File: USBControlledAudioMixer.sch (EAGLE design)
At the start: 36 parts, among them IC1 TDA7448, IC2 TS912, IC3 MEGA8-AI, J1 MOLEX 47346-0001, J2 AVR_SPI_PRG_6NS

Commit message: Minor update (sorry for nonsense commit message)
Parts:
- removed D2: BZX84CSMD, diode:BZX84CSMD
- removed LED6, LED7, LED8: (no value), led:LEDCHIPLED-0603-TTW
- added D3: (no value), diode:DIODE-2CA|ACSOT23
- added IC4: OPA344N-SOT23, linear:OPA344N-SOT23
- added JP1: (no value), pinhead:PINHD-1X4/90
- added L1: (no value), rcl:L-EUL3225M
- added R10, R11, R6, R7, R8, R9: (no value), rcl:R-EU_R0603
- added R12: 470, rcl:R-EU_R0603
- added R13, R14: 62, rcl:R-EU_R0603
- added R15: 1k5, rcl:R-EU_R0603
- added U$1: 470, Simplex-rlc:RES_ARR
- C1: value 22p -> 12p; device rcl:C-EUC0805K -> rcl:C-EUC0603; OC_DIGIKEY (none) -> 1276-1254-1-ND; OC_TME CL21C220JBANNNC -> (none); PRICE_100 (none) -> 0.013
- C10, C11, C6, C7, C8, C9: value 22p -> 470n; device rcl:C-EUC0805K -> rcl:C-EUC0603; OC_DIGIKEY (none) -> 1276-2377-1-ND; OC_TME CL21C220JBANNNC -> (none); PRICE_100 (none) -> 0.017
- C2: value 22p -> 12p; device rcl:C-EUC0805K -> rcl:C-EUC0603
- C3: device rcl:C-EUC0805K -> rcl:C-EUC0603; OC_DIGIKEY (none) -> 1276-1258-1-ND; OC_TME CC0805JRX7R9104 -> (none); PRICE_100 (none) -> 0.008
- C4: device rcl:CPOL-EUA/3216-18W -> rcl:CPOL-EUSMCA; OC_TME TAJA106M010R -> TAJA155K016R; PRICE_100 (none) -> 0.059
- D1: value BZX84CSMD -> (none); device diode:BZX84CSMD -> diode:DIODE-SOD123; OC_TME BZX84C3V6-DIO -> (none)
- IC3: OC_TME (none) -> ATMEGA8-16AU; PRICE_10 (none) -> 1.37
- LED1, LED2, LED3, LED4, LED5: OC_TME (none) -> KPA-1606QBC-F; PRICE_100 (none) -> 0.2511
- Q1: value (none) -> 16MHz; device crystal:CRYSTALHC49UP -> nonolith:CRYSTALTHIN; OC_DIGIKEY (none) -> SER3628CT-ND; PRICE_10 (none) -> 0.53
- R3: device rcl:R-EU_R0805 -> rcl:R-EU_R0603
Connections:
- new net LED1: IC3.PD6(AIN0), LED1.A
- new net LED2: IC3.PD7(AIN1), LED2.A
- new net LED3: IC3.PB0(ICP), LED3.A
- new net LED4: IC3.PB1(OC1A), LED4.A
- new net LED5: IC3.PB2(SS/OC1B), LED5.A
- new net N$11: D3.K2, JP1.2, R13.2, R15.2
- new net N$13: D3.K1, JP1.3, R14.2
- new net N$5: LED1.C, U$1.8
- new net N$6: LED2.C, U$1.7
- new net N$7: LED3.C, U$1.6
- new net N$8: LED4.C, U$1.5
- new net N$9: LED5.C, R12.2
- net +5V: now also JP1.1, R15.1
- net D+: now also IC3.PD2(INT0), R14.1; no longer IC3.PC1(ADC1)
- net D-: now also IC3.PD4(XCK/T0), R13.1; no longer IC3.PC0(ADC0)
- net GND: now also D3.A, JP1.4, R12.1, U$1.1, U$1.2, U$1.3, U$1.4
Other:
- note added: "Load Capacitance = 9pF Req. Capacitors = 14pF Next Value = 12pF"
- moved on the sheet: C10, C11, C5, C6, C7, C8, C9, IC1, LED1, LED2, LED3, LED4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

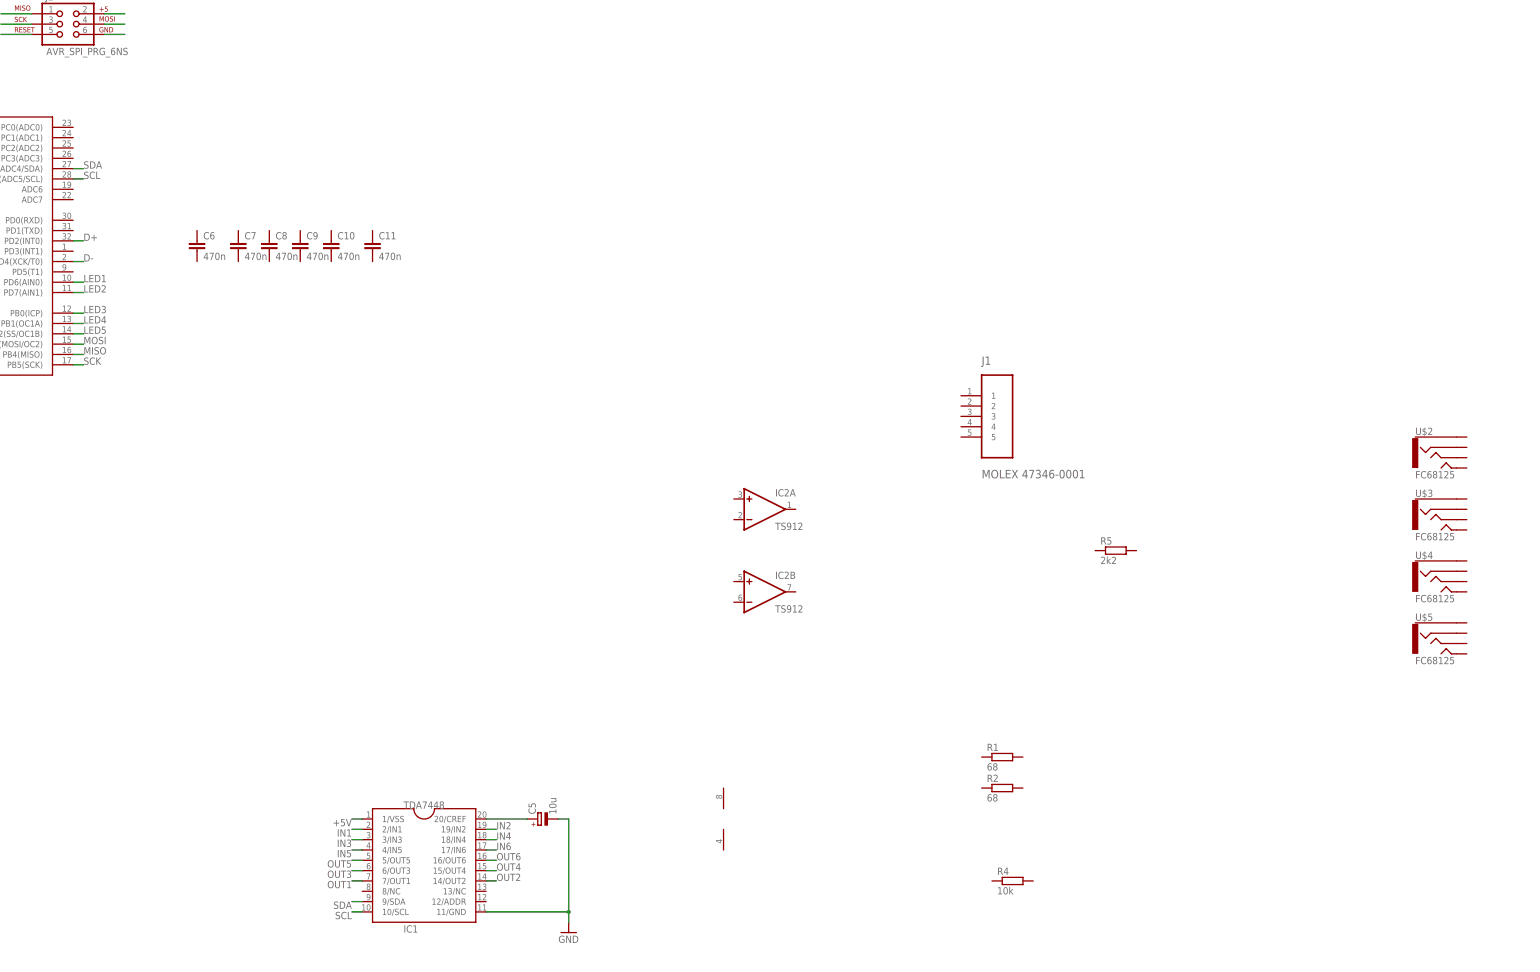
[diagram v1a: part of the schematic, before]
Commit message: Added LEDs an basic wiring
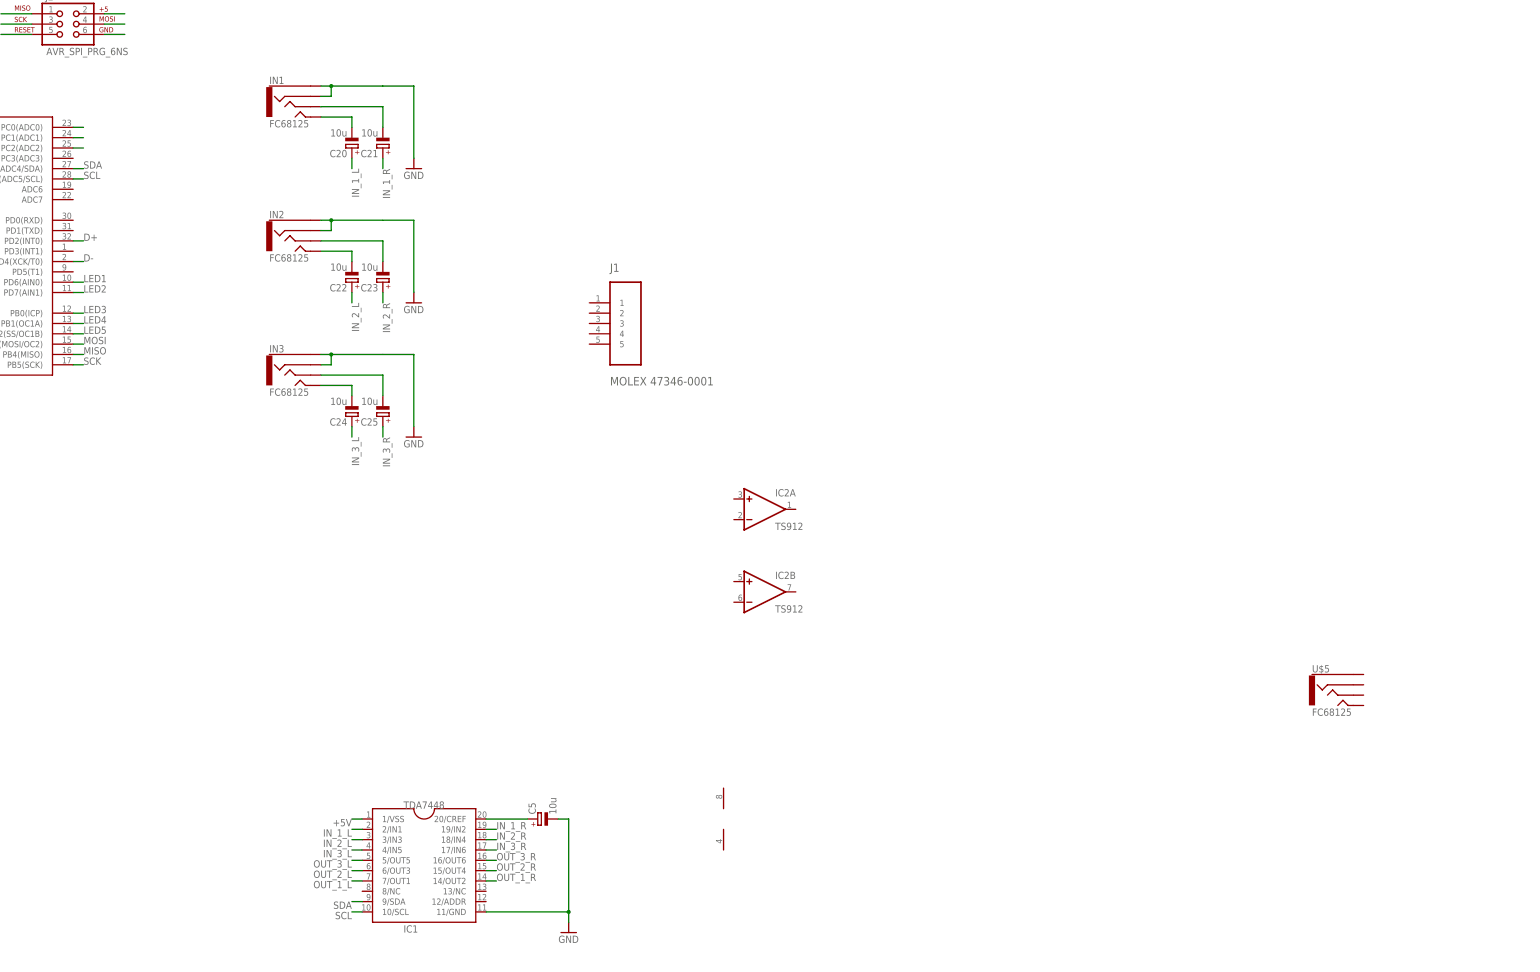
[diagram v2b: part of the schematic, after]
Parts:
- removed C10, C11, C6, C7, C8, C9: 470n, rcl:C-EUC0603
- removed R1, R2: 68, rcl:R-EU_R0805
- removed R4: 10k, rcl:R-EU_R0805
- removed R5: 2k2, rcl:R-EU_R0805
- removed U$2, U$3, U$4: FC68125, FC68125:FC68125
- added C20, C21, C22, C23, C24, C25: 10u, rcl:CPOL-EU153CLV-0405
- added IN1, IN2, IN3: FC68125, FC68125:FC68125
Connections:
- net OUT1 renamed OUT_1_L
- net OUT2 renamed OUT_1_R
- net OUT3 renamed OUT_2_L
- net OUT4 renamed OUT_2_R
- net OUT5 renamed OUT_3_L
- net OUT6 renamed OUT_3_R
- removed net IN1: IC1.2/IN1
- removed net IN2: IC1.19/IN2
- removed net IN3: IC1.3/IN3
- removed net IN4: IC1.18/IN4
- removed net IN5: IC1.4/IN5
- removed net IN6: IC1.17/IN6
- new net IN_1_L: C20.+, IC1.2/IN1
- new net IN_1_R: C21.+, IC1.19/IN2
- new net IN_2_L: C22.+, IC1.3/IN3
- new net IN_2_R: C23.+, IC1.18/IN4
- new net IN_3_L: C24.+, IC1.4/IN5
- new net IN_3_R: C25.+, IC1.17/IN6
- new net N$10: C24.-, IN3.4
- new net N$12: C25.-, IN3.3
- new net N$14: C22.-, IN2.4
- new net N$15: C23.-, IN2.3
- new net N$16: C20.-, IN1.4
- new net N$17: C21.-, IN1.3
- new net N$18: IC3.PC0(ADC0)
- new net N$19: IC3.PC1(ADC1)
- new net N$20: IC3.PC2(ADC2)
- net GND: now also IN1.1, IN1.2, IN2.1, IN2.2, IN3.1, IN3.2
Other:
- moved on the sheet: J1, U$5

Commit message: Pre-final version without proper board layout
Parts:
- removed D1: (no value), diode:DIODE-SOD123
- removed IC4: OPA344N-SOT23, linear:OPA344N-SOT23
- removed JP1: (no value), pinhead:PINHD-1X4/90
- removed L1: (no value), rcl:L-EUL3225M
- removed R10, R11, R6, R7, R8, R9: (no value), rcl:R-EU_R0603
- added C10, C9: 10u, rcl:CPOL-EU153CLV-0405
- added C11: 100n, rcl:C-EUC0603
- added C6: 10µ, rcl:C-EUC0805
- added C7: 2.2µ, rcl:C-EUC0603
- added C8: 330p, rcl:C-EUC0603
- added D2: (no value), adafruit:DIODESOD-123
- added JP2: (no value), pinhead:PINHD-1X3/90
- added L2: (no value), SparkFun:INDUCTOR1007
- added R1, R16, R17, R5: 1M, rcl:R-EU_R0603
- added R18, R19, R20: 1k, rcl:R-EU_R0603
- added R2: 13.3k, rcl:R-EU_R0603
- added R4: 84.5k, rcl:R-EU_R0603
- added U1: LMR62014, projectLibrary:LMR62014
- J1: value MOLEX 47346-0001 -> (none); OC_TME MX-47346-0001 -> (none)
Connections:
- removed net OUT_1_L: IC1.7/OUT1
- removed net OUT_1_R: IC1.14/OUT2
- removed net OUT_2_L: IC1.6/OUT3
- removed net OUT_2_R: IC1.15/OUT4
- removed net OUT_3_L: IC1.5/OUT5
- removed net OUT_3_R: IC1.16/OUT6
- new net +9V: C6.1, C8.2, D2.C, R4.1
- new net N$21: R1.2, U1.SHDN
- new net N$22: D2.A, L2.2, U1.SW
- new net N$23: C9.-, U$5.4
- new net N$24: C9.+, IC2A.-IN, IC2A.OUT
- new net N$25: C8.1, R2.2, R4.2, U1.FB
- new net N$26: C10.-, U$5.3
- new net N$27: IC2B.+IN
- new net OUT_L: IC1.5/OUT5, IC1.6/OUT3, IC1.7/OUT1, IC2A.+IN
- new net OUT_R: C10.+, IC1.14/OUT2, IC1.15/OUT4, IC1.16/OUT6, IC2B.-IN, IC2B.OUT
- new net TOUCH_RCV_+: IC3.PC0(ADC0), R19.1
- new net TOUCH_RCV_-: IC3.PC1(ADC1), R18.1
- new net TOUCH_RCV_CHAN: IC3.PC2(ADC2), R20.1
- new net TOUCH_SEND_+: IC3.PC3(ADC3), R16.1
- new net TOUCH_SEND_-: IC3.PD3(INT1), R5.1
- new net TOUCH_SEND_CHAN: IC3.PD5(T1), R17.1
- net +5V: now also C11.1, C7.1, IC2P.V+, J1.1, L2.1, R1.1, U1.VIN; no longer JP1.1
- net GND: now also C11.2, C6.2, C7.2, IC2P.V-, J1.5, R2.1, U$5.1, U1.GND; no longer JP1.4
- net N$11: now also D3.K1, J1.2; no longer D3.K2, JP1.2
- net N$13: now also D3.K2, J1.3; no longer D3.K1, JP1.3
- net N$18: now also JP2.1, R18.2, R5.2; no longer IC3.PC0(ADC0)
- net N$19: now also JP2.2, R16.2, R19.2; no longer IC3.PC1(ADC1)
- net N$20: now also JP2.3, R17.2, R20.2; no longer IC3.PC2(ADC2)
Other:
- moved on the sheet: IC2A, IC2B, J1, U$5
